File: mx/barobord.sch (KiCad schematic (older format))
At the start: 147 parts, among them J1 Pimoroni, SW1 SW_Push, SW10 SW_Push, SW11 SW_Push, SW12 SW_Push, SW13 SW_Push, SW14 SW_Push, SW15 SW_Push, SW16 SW_Push, SW17 SW_Push, SW18 SW_Push, SW19 SW_Push, SW2 SW_Push, SW20 SW_Push, SW21 SW_Push, SW22 SW_Push, SW23 SW_Push, SW24 SW_Push, SW25 SW_Push, SW26 SW_Push, SW27 SW_Push, SW28 SW_Push, SW29 SW_Push, SW3 SW_Push, SW30 SW_Push, SW31 SW_Push, SW32 SW_Push, SW33 SW_Push, SW34 SW_Push, SW35 SW_Push, SW36 SW_Push, SW37 SW_Push, SW38 SW_Push, SW39 SW_Push, SW4 SW_Push, SW40 SW_Push, SW41 SW_Push, SW42 RotaryEncoder_Switch, SW43 RotaryEncoder_Switch, SW44 EVQWGD001, SW45 EVQWGD001, SW5 SW_Push, SW6 SW_Push, SW7 SW_Push, SW8 SW_Push, SW9 SW_Push, U1 ATmega32U4-A, U2 PRTR5V0U2X, Y1 Crystal_GND24_Small

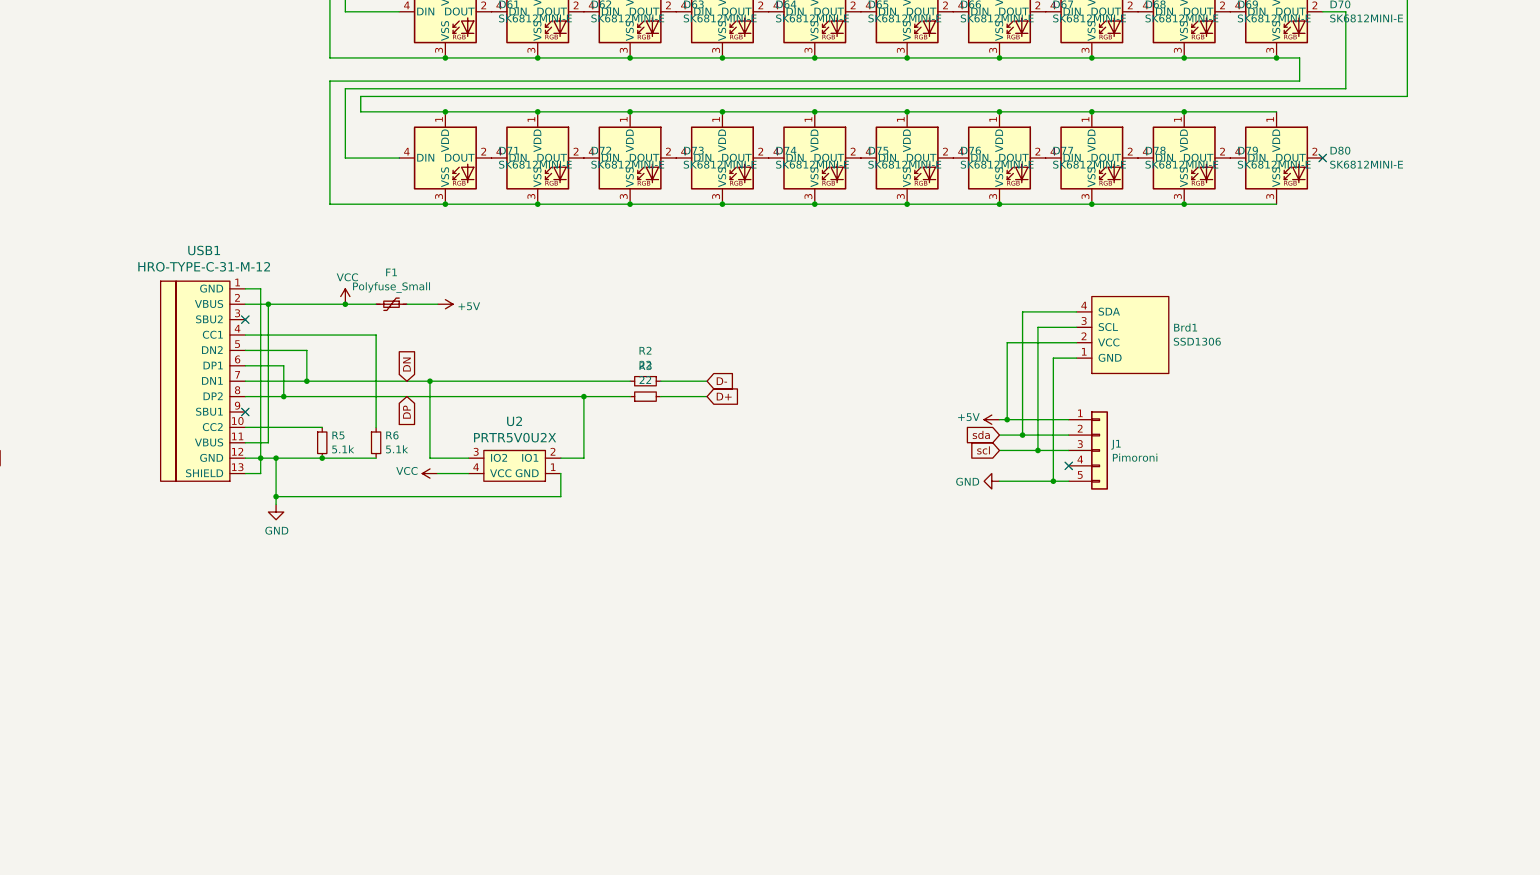
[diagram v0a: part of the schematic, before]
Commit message: added underglow support for the MX version (not byo-mcu or choc)
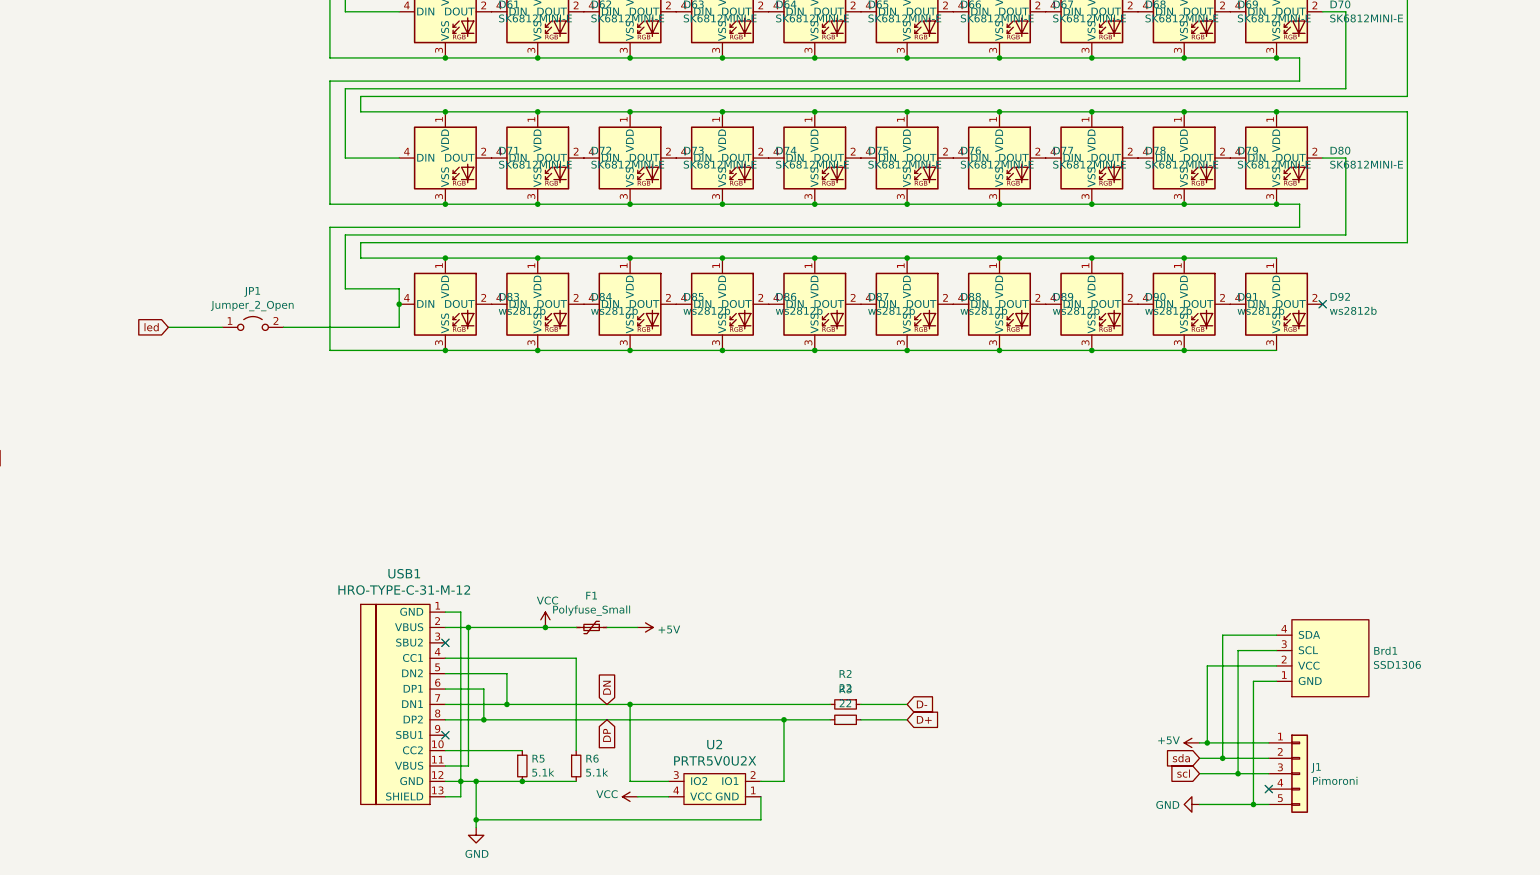
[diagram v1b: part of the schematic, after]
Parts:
- added D83, D84, D85, D86, D87, D88, D89, D90, D91, D92: ws2812b, Keebio-Parts:WS2812B, symbol kicad-keyboard-parts:SK6812MINI-E
- added JP1: Jumper_2_Open, Jumper:SolderJumper-2_P1.3mm_Open_RoundedPad1.0x1.5mm, symbol Jumper:Jumper_2_Open
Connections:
- net +5V: now also D83.1 (VDD), D84.1 (VDD), D85.1 (VDD), D86.1 (VDD), D87.1 (VDD), D88.1 (VDD), D89.1 (VDD), D90.1 (VDD), D91.1 (VDD), D92.1 (VDD)
- net GND: now also D83.3 (VSS), D84.3 (VSS), D85.3 (VSS), D86.3 (VSS), D87.3 (VSS), D88.3 (VSS), D89.3 (VSS), D90.3 (VSS), D91.3 (VSS), D92.3 (VSS)
- net led: now also JP1.1 (A)
- net at D80.2 (DOUT): now also D83.4 (DIN), JP1.2 (B)
- new net: D83.2 (DOUT), D84.4 (DIN)
- new net: D84.2 (DOUT), D85.4 (DIN)
- new net: D85.2 (DOUT), D86.4 (DIN)
- new net: D86.2 (DOUT), D87.4 (DIN)
- new net: D87.2 (DOUT), D88.4 (DIN)
- new net: D88.2 (DOUT), D89.4 (DIN)
- new net: D89.2 (DOUT), D90.4 (DIN)
- new net: D90.2 (DOUT), D91.4 (DIN)
- new net: D91.2 (DOUT), D92.4 (DIN)
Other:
- moved on the sheet: Brd1, F1, J1, R2, R3, R5, R6, U2, USB1
